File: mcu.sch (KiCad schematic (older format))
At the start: 50 parts, among them J11 RJ45_Shielded, J13 HR911105A, J2 RJ45_Shielded, U3 STM32F207VGT6, U4 MCP2562-E-P, U5 LAN8720A, Y1 Crystal_GND24

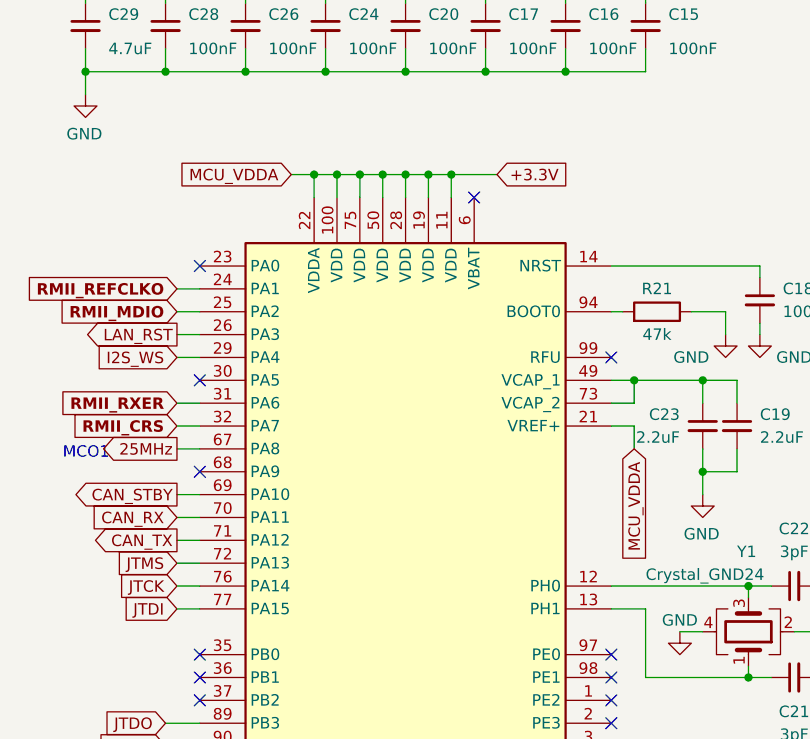
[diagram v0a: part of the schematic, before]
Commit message: further re-arrangement, PCB is now 100x90 mm² \o/. A bit more placement to do, then back to routing :>
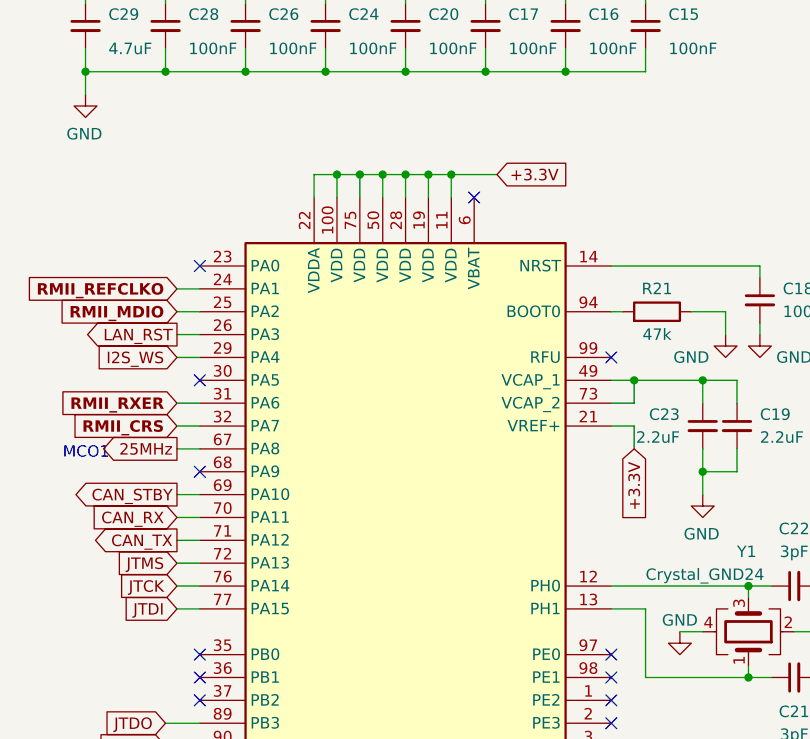
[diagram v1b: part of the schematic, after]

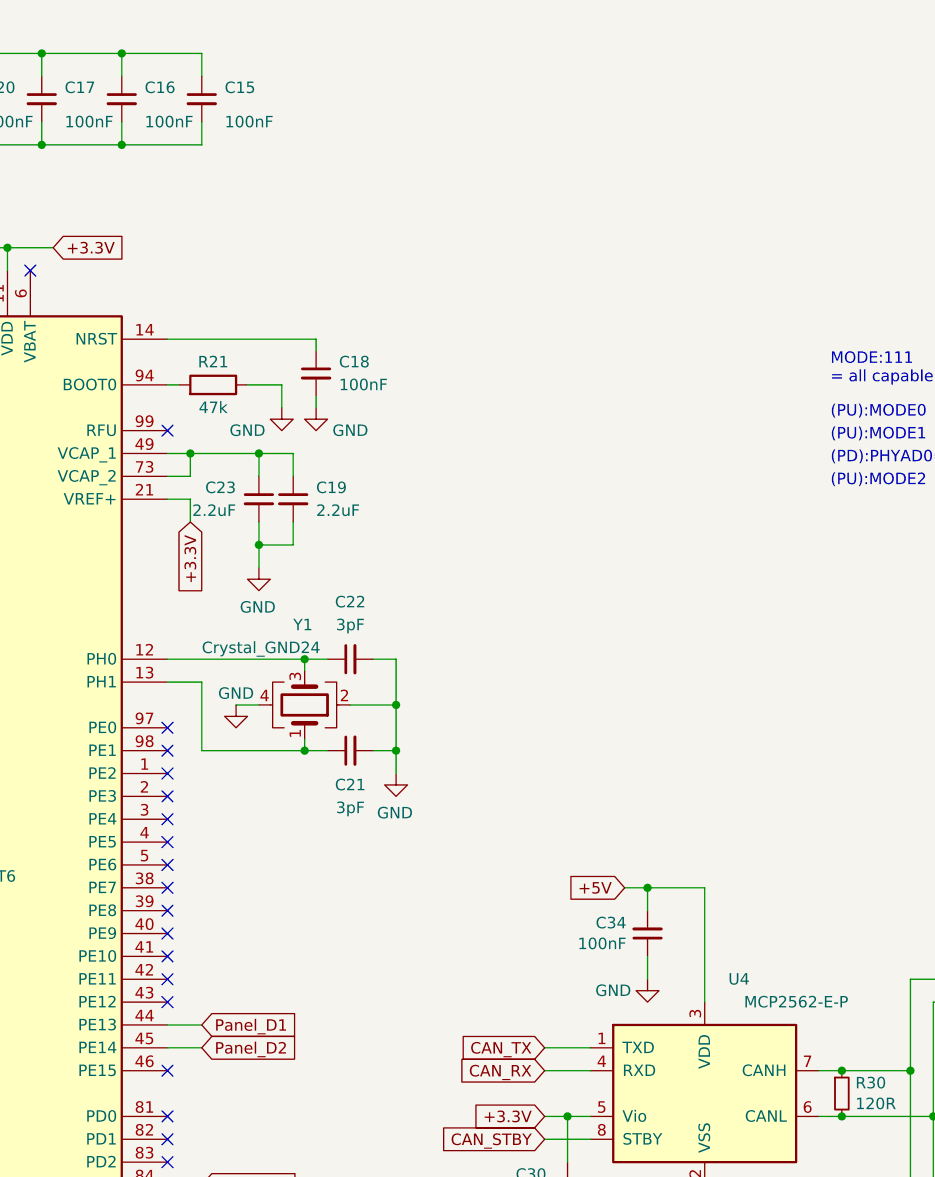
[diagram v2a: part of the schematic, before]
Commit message: Add LEDs, tweak MOSFET sink.
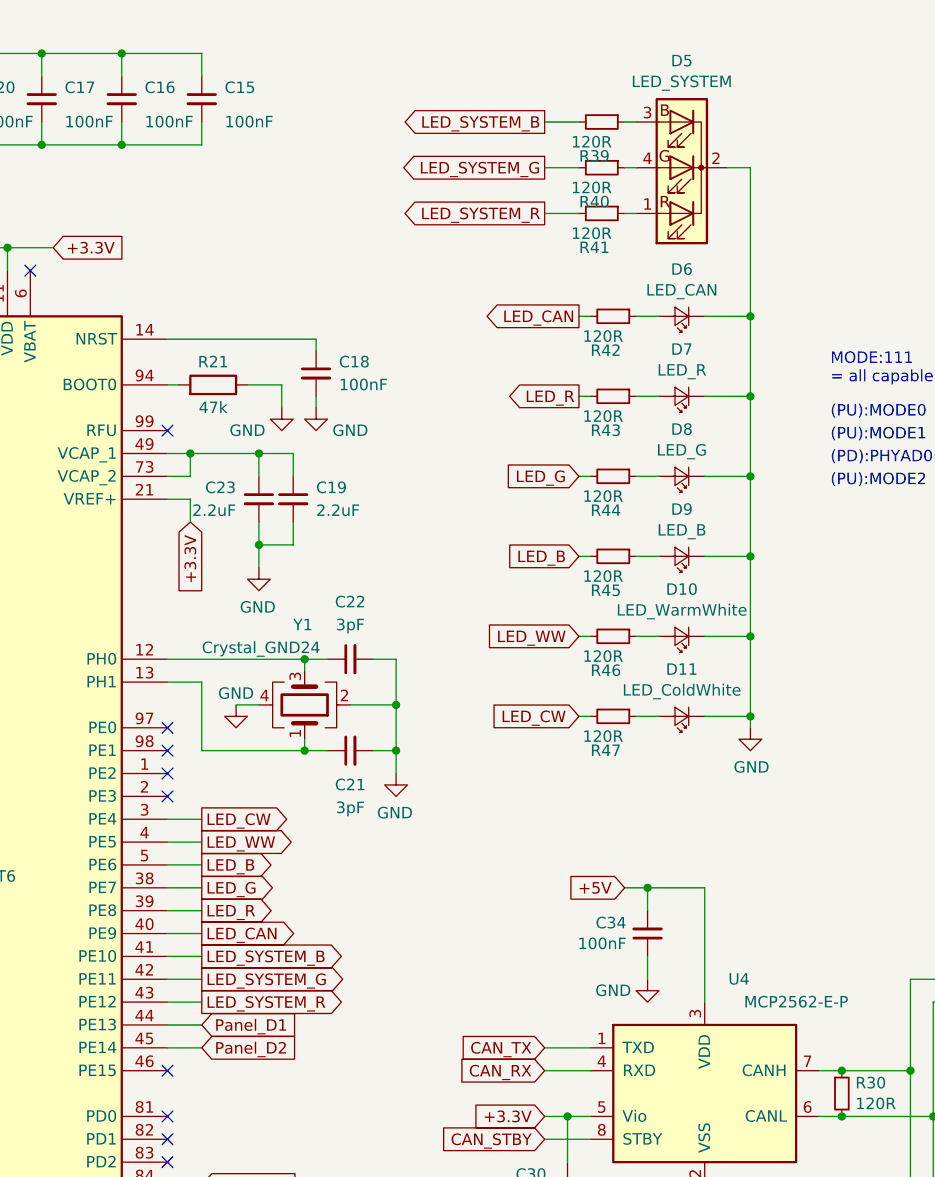
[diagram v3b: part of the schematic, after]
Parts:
- added D10: LED_WarmWhite, LED_SMD:LED_0603_1608Metric_Castellated, symbol Device:LED_Small
- added D11: LED_ColdWhite, LED_SMD:LED_0603_1608Metric_Castellated, symbol Device:LED_Small
- added D5: LED_SYSTEM, LED_SMD:LED_Cree-PLCC4_2x2mm_CW, symbol Device:LED_RCBG
- added D6: LED_CAN, LED_SMD:LED_0603_1608Metric_Castellated, symbol Device:LED_Small
- added D7: LED_R, LED_SMD:LED_0603_1608Metric_Castellated, symbol Device:LED_Small
- added D8: LED_G, LED_SMD:LED_0603_1608Metric_Castellated, symbol Device:LED_Small
- added D9: LED_B, LED_SMD:LED_0603_1608Metric_Castellated, symbol Device:LED_Small
- added R39, R40, R41, R42, R43, R44, R45, R46, R47: 120R, Resistor_SMD:R_0603_1608Metric, symbol Device:R_Small
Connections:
- net GND: now also D10.1 (K), D11.1 (K), D5.2 (K), D6.1 (K), D7.1 (K), D8.1 (K), D9.1 (K)
- net LED_CW: now reaches U3.3 (PE4)
- net LED_CW: now also R47.2
- net LED_G: now reaches U3.38 (PE7)
- net LED_G: now also R44.2
- net LED_R: now reaches U3.39 (PE8)
- net LED_R: now also R43.2
- net LED_WW: now reaches U3.4 (PE5)
- net LED_WW: now also R46.2
- net LED_CAN: now reaches U3.40 (PE9)
- net LED_CAN: now also R42.2
- net LED_SYSTEM_B: now reaches U3.41 (PE10)
- net LED_SYSTEM_B: now also R39.2
- net LED_SYSTEM_G: now reaches U3.42 (PE11)
- net LED_SYSTEM_G: now also R40.2
- net LED_SYSTEM_R: now reaches U3.43 (PE12)
- net LED_SYSTEM_R: now also R41.2
- net LED_B: now reaches U3.5 (PE6)
- net LED_B: now also R45.2
- new net: D5.1 (RA), R41.1
- new net: D5.3 (BA), R39.1
- new net: D5.4 (GA), R40.1
- new net: D6.2 (A), R42.1
- new net: D7.2 (A), R43.1
- new net: D10.2 (A), R46.1
- new net: D11.2 (A), R47.1
- new net: D8.2 (A), R44.1
- new net: D9.2 (A), R45.1
- no-connect marks 48 -> 39

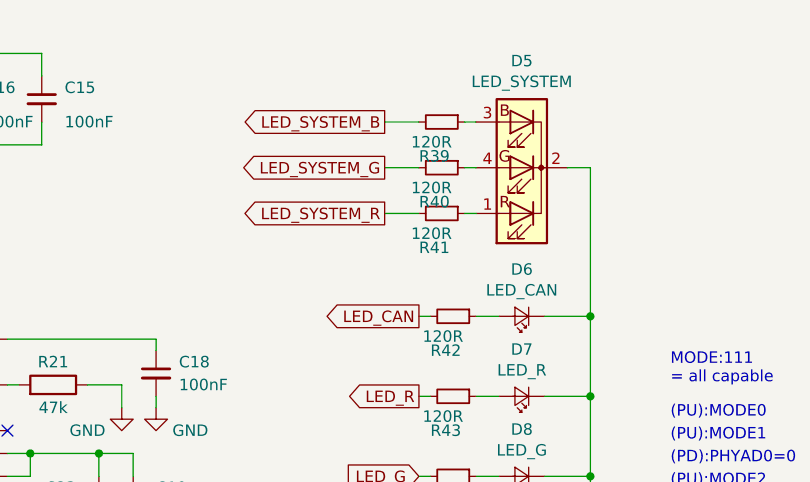
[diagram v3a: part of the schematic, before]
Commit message: 3.3V buck converter now connected to 12V (prep for 48V>12V upgrade regarding IoP applicability)
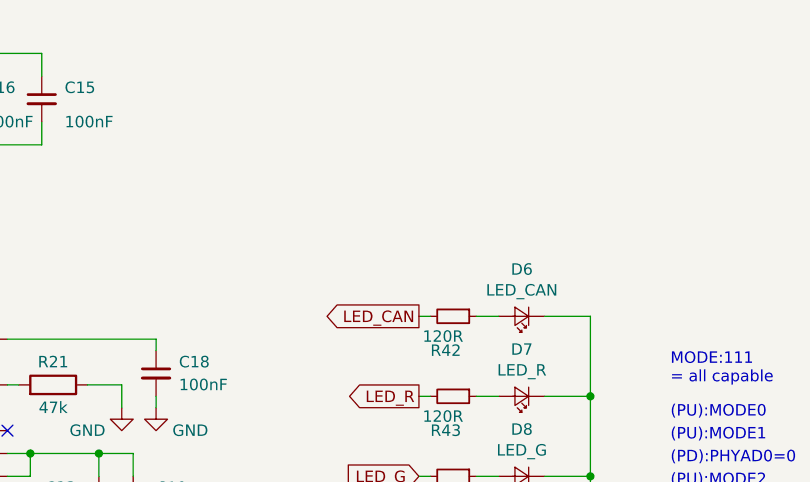
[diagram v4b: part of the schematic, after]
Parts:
- removed D5: LED_SYSTEM, LED_SMD:LED_Cree-PLCC4_2x2mm_CW, symbol Device:LED_RCBG
- removed R39, R40, R41: 120R, Resistor_SMD:R_0603_1608Metric, symbol Device:R_Small
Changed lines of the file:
@@
 EESchema Schematic File Version 4
 LIBS:panel_light_control-cache
-EELAYER 26 0
+EELAYER 28 0
 EELAYER END
 $Descr A4 11693 8268
@@
 +3.3V
 $Comp
-L Device:LED_RCBG D5
-U 1 1 5BD4129E
-P 5650 1250
-F 0 "D5" H 5650 783 50  0000 C CNN
-F 1 "LED_SYSTEM" H 5650 874 50  0000 C CNN
-F 2 "LED_SMD:LED_Cree-PLCC4_2x2mm_CW" H 5650 1200 50  0001 C CNN
-F 3 "~" H 5650 1200 50  0001 C CNN
-F 4 "ASMB-KTF0-0A306 " H 5650 1250 50  0001 C CNN "MPN"
-F 5 "630-ASMB-KTF0-0A306 " H 5650 1250 50  0001 C CNN "Mouser"
-	1    5650 1250
-	-1   0    0    1
-$EndComp
-$Comp
 L Device:LED_Small D6
 U 1 1 5BD41B70
@@
 Text GLabel 3550 4800 2    50   Output ~ 0
 LED_SYSTEM_G
-Text GLabel 5050 1450 0    50   Output ~ 0
-LED_SYSTEM_R
 $Comp
 L power:GND #PWR0113
@@
 $EndComp
 Wire Wire Line
-	5850 1250 5950 1250
-Wire Wire Line
 	5750 1900 5950 1900
 Wire Wire Line
@@
 Wire Wire Line
 	5450 3650 5550 3650
-Connection ~ 5950 1900
-Text GLabel 5050 1250 0    50   Output ~ 0
-LED_SYSTEM_G
-Text GLabel 5050 1050 0    50   Output ~ 0
-LED_SYSTEM_B
 Text GLabel 3550 4600 2    50   Output ~ 0
 LED_CAN
@@
 Wire Wire Line
 	5200 3650 5250 3650
-Wire Wire Line
-	5950 1250 5950 1900
-$Comp
-L Device:R_Small R41
-U 1 1 5C185C5D
-P 5300 1450
-AR Path="/5BBC4BB7/5C185C5D" Ref="R41"  Part="1"
-AR Path="/5C1EFDBE/5C185C5D" Ref="R?"  Part="1"
-AR Path="/5C211DD3/5C185C5D" Ref="R?"  Part="1"
-AR Path="/5C211FC6/5C185C5D" Ref="R?"  Part="1"
-F 0 "R41" V 5450 1350 50  0000 L CNN
-F 1 "120R" V 5359 1405 50  0000 C TNN
-F 2 "Resistor_SMD:R_0603_1608Metric" H 5300 1450 50  0001 C CNN
-F 3 "~" H 5300 1450 50  0001 C CNN
-	1    5300 1450
-	0    1    1    0
-$EndComp
-$Comp
-L Device:R_Small R40
-U 1 1 5C185CFF
-P 5300 1250
-AR Path="/5BBC4BB7/5C185CFF" Ref="R40"  Part="1"
-AR Path="/5C1EFDBE/5C185CFF" Ref="R?"  Part="1"
-AR Path="/5C211DD3/5C185CFF" Ref="R?"  Part="1"
-AR Path="/5C211FC6/5C185CFF" Ref="R?"  Part="1"
-F 0 "R40" V 5450 1150 50  0000 L CNN
-F 1 "120R" V 5359 1205 50  0000 C TNN
-F 2 "Resistor_SMD:R_0603_1608Metric" H 5300 1250 50  0001 C CNN
-F 3 "~" H 5300 1250 50  0001 C CNN
-	1    5300 1250
-	0    1    1    0
-$EndComp
-$Comp
-L Device:R_Small R39
-U 1 1 5C185D99
-P 5300 1050
-AR Path="/5BBC4BB7/5C185D99" Ref="R39"  Part="1"
-AR Path="/5C1EFDBE/5C185D99" Ref="R?"  Part="1"
-AR Path="/5C211DD3/5C185D99" Ref="R?"  Part="1"
-AR Path="/5C211FC6/5C185D99" Ref="R?"  Part="1"
-F 0 "R39" V 5450 950 50  0000 L CNN
-F 1 "120R" V 5359 1005 50  0000 C TNN
-F 2 "Resistor_SMD:R_0603_1608Metric" H 5300 1050 50  0001 C CNN
-F 3 "~" H 5300 1050 50  0001 C CNN
-	1    5300 1050
-	0    1    1    0
-$EndComp
-Wire Wire Line
-	5050 1050 5200 1050
-Wire Wire Line
-	5050 1250 5200 1250
-Wire Wire Line
-	5050 1450 5200 1450
-Wire Wire Line
-	5450 1450 5400 1450
-Wire Wire Line
-	5400 1250 5450 1250
-Wire Wire Line
-	5450 1050 5400 1050
 Text GLabel 3550 4500 2    50   Output ~ 0
 LED_R
